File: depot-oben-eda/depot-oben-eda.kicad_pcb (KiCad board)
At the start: 2 copper layers, 45 x 45 mm, 13 parts, among them J1 SUPPLY, J2 RPi, J3 Schnapper, Q1 BSP76

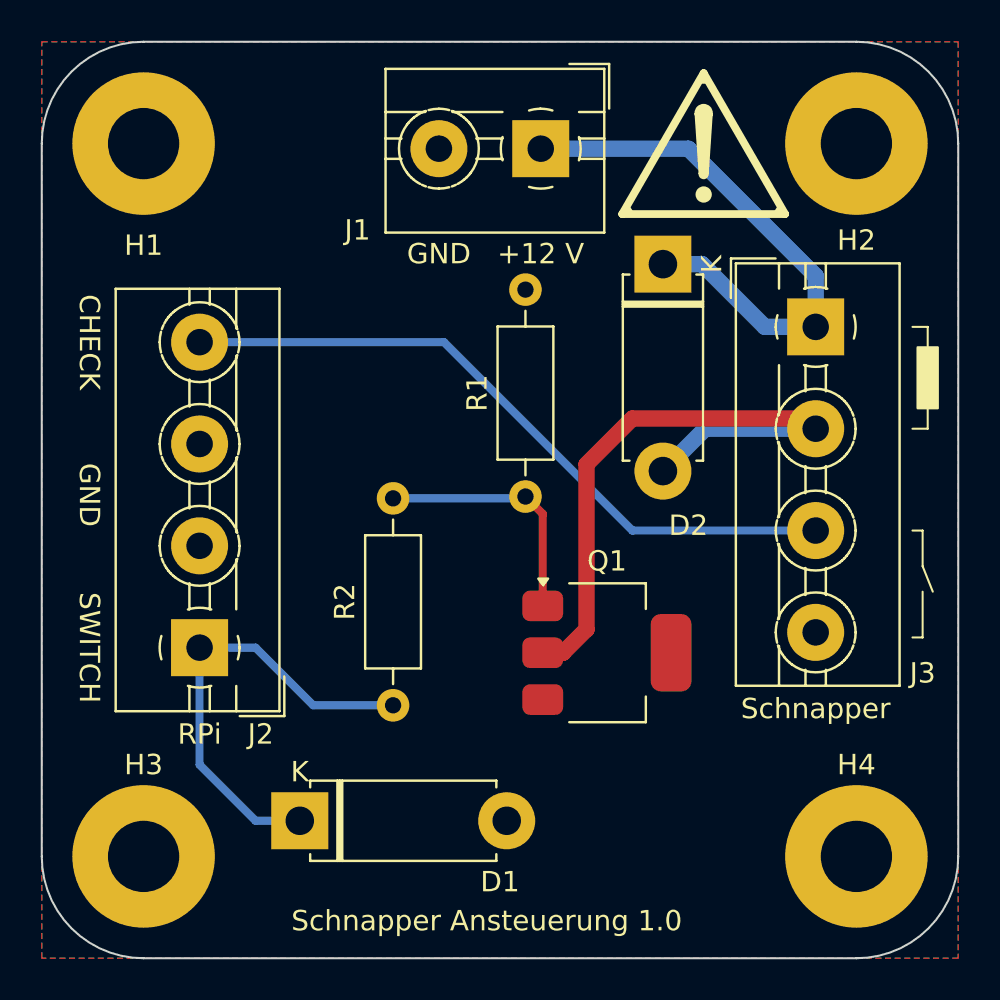
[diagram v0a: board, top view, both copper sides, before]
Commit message: * Change footprint of BSP76 to have D on Pin 4 * Move silkscreen of supply terminal down * increase GND spoke width
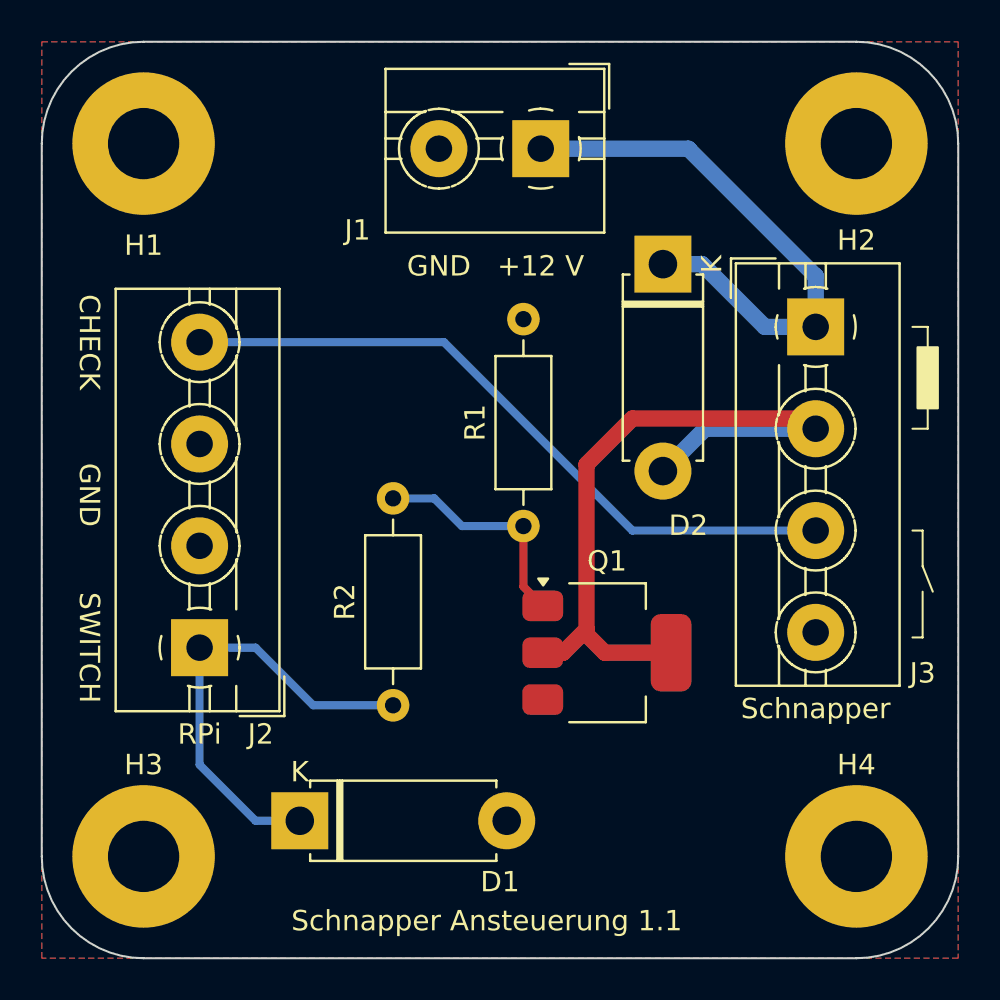
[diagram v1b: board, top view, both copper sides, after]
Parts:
- removed REF**: Symbol_Attention_Triangle_8x7mm_Copper, Symbol:Symbol_Attention_Triangle_8x7mm_Copper
- Q1: footprint Package_TO_SOT_SMD:SOT-223 -> Package_TO_SOT_SMD:SOT-223-3_TabPin2
- moved R1 1.45 mm to (146.9, 92.3)
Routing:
- net /BSP_DRAIN: track 31.5 -> 36.2 mm
- net Net-(Q1-G): track 12.3 -> 11.3 mm
